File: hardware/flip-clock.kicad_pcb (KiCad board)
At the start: 2 copper layers, 68.1 x 38.6 mm, 9 parts, among them J1 Screw_Terminal_01x02, U1 ESP-01v090, U2 AP1117-33

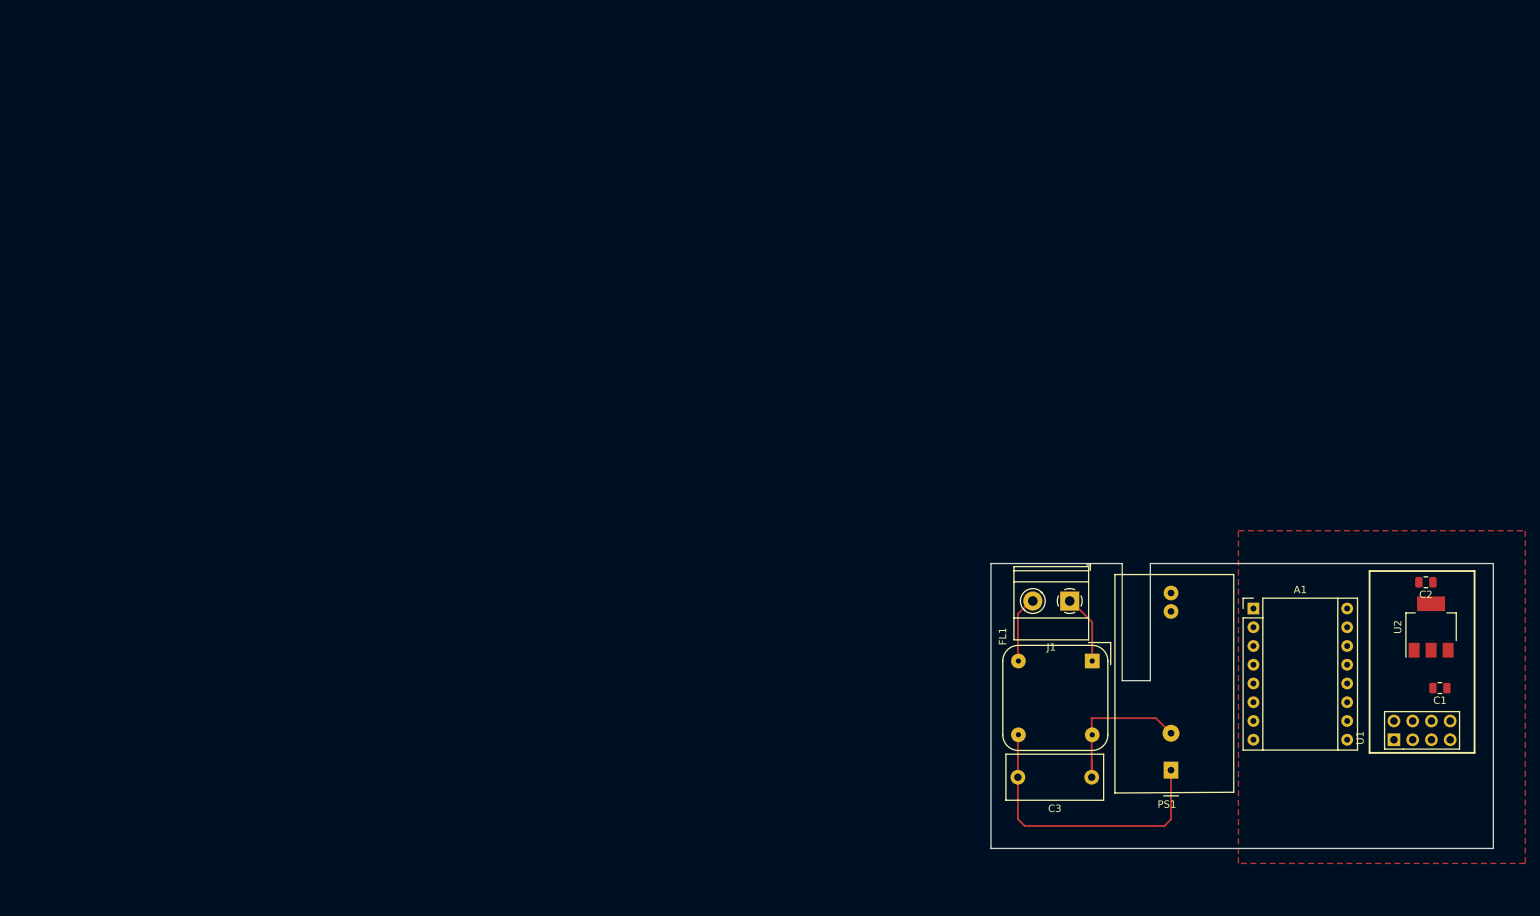
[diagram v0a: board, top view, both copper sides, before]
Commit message: Layout without choke
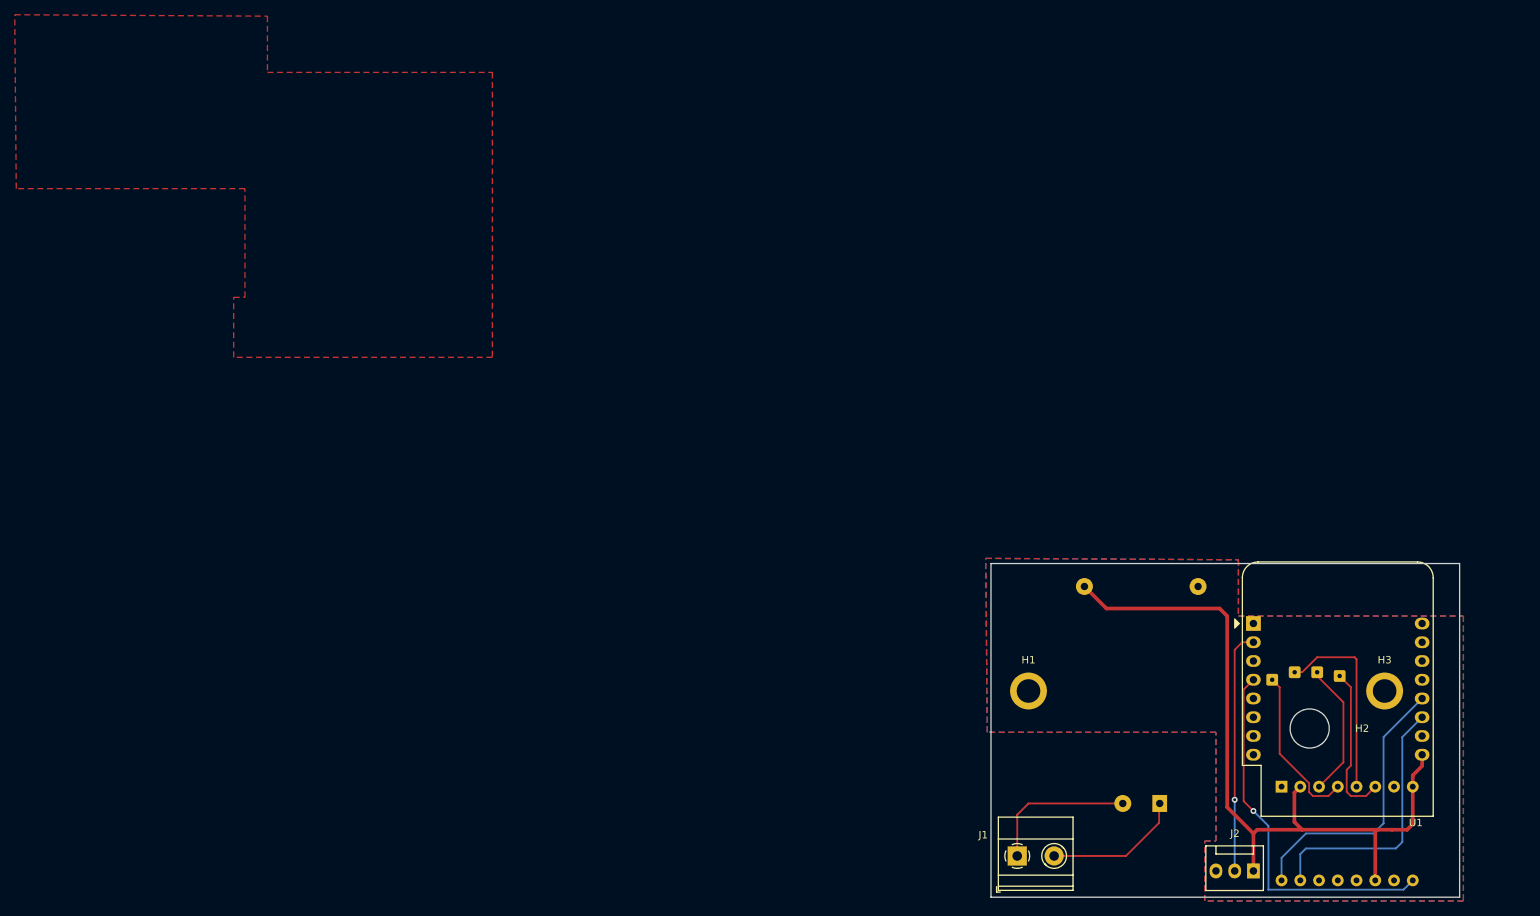
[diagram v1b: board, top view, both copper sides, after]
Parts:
- removed C1, C2: C, Capacitor_SMD:C_0805_2012Metric
- removed C3: C, Capacitor_THT:C_Rect_L13.0mm_W6.0mm_P10.00mm_FKS3_FKP3_MKS4
- removed FL1: Choke_Schaffner_RN102-0.3-02-12M, Inductor_THT:Choke_Schaffner_RN102-04-14.0x14.0mm
- removed U2: AP1117-33, Package_TO_SOT_SMD:SOT-223-3_TabPin2
- added H-1A1: MountingHole_Pad, Connector_Wire:SolderWire-0.1sqmm_1x01_D0.4mm_OD1mm, B.Cu at (160.0, 66.5)
- added H-1B1: MountingHole_Pad, Connector_Wire:SolderWire-0.1sqmm_1x01_D0.4mm_OD1mm, B.Cu at (166.1, 65.5)
- added H-2A1: MountingHole_Pad, Connector_Wire:SolderWire-0.1sqmm_1x01_D0.4mm_OD1mm, B.Cu at (163.1, 65.5)
- added H-2B1: MountingHole_Pad, Connector_Wire:SolderWire-0.1sqmm_1x01_D0.4mm_OD1mm, B.Cu at (169.2, 66.0)
- added H1: MountingHole, MountingHole:MountingHole_3.2mm_M3, F.Cu at (127.0, 68.1)
- added H2: MountingHole, MountingHole:MountingHole_5.3mm_M5, F.Cu at (165.1, 73.2)
- added H3: MountingHole, MountingHole:MountingHole_3.2mm_M3, F.Cu at (175.3, 68.1)
- added J2: Conn_01x03_Female, Connector:FanPinHeader_1x03_P2.54mm_Vertical, F.Cu at (157.5, 92.5)
- A1: moved to B.Cu
- PS1: footprint Converter_ACDC:Converter_ACDC_HiLink_HLK-2Mxx -> Converter_ACDC:Converter_ACDC_HiLink_HLK-PMxx; moved to B.Cu
- U1: value ESP-01v090 -> WeMos_D1_mini; footprint ESP:ESP-01 -> Module:WEMOS_D1_mini_light
- moved J1 35.3 mm to (125.5, 90.4), turned to 0 degrees
- moved U1 24.7 mm to (157.5, 58.9), turned to 0 degrees
- moved A1 24.4 mm to (161.3, 81.0), turned to -90 degrees
- moved PS1 4.11 mm to (144.8, 83.3)
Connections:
- A1 pad 10: /3V3 -> unconnected-(A1-Pad10)
- A1 pad 11: /3V3 -> VCC
- A1 pad 12: /3V3 -> unconnected-(A1-Pad12)
- A1 pad 13: Net-(A1-Pad13) -> unconnected-(A1-Pad13)
- A1 pad 16: GND -> /DIR
- A1 pad 2: /3V3 -> VCC
- A1 pad 3: unconnected-(A1-Pad3) -> /1B
- A1 pad 4: unconnected-(A1-Pad4) -> /1A
- A1 pad 5: unconnected-(A1-Pad5) -> /2A
- A1 pad 6: unconnected-(A1-Pad6) -> /2B
- A1 pad 9: GND -> //ENABLE
- J1 pad 1: Net-(FL1-Pad1) -> /AC1
- J1 pad 2: Net-(FL1-Pad3) -> /AC2
- PS1 pad 1: Net-(PS1-Pad1) -> /AC2
- PS1 pad 2: Net-(PS1-Pad2) -> /AC1
- U1 pad 1: Net-(A1-Pad13) -> unconnected-(U1-Pad1)
- U1 pad 2: GND -> /PD_IN
- U1 pad 4: /STEP -> //ENABLE
- U1 pad 7: /3V3 -> unconnected-(U1-Pad7)
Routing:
- net VCC: track 0.00 -> 102.6 mm
- net //ENABLE: track 0.00 -> 50.5 mm, vias 0 -> 1
- net Net-(PS1-Pad1): track 39.6 -> 0.00 mm
- net /DIR: track 0.00 -> 37.9 mm
- net /STEP: track 0.00 -> 36.1 mm
- net /PD_IN: track 0.00 -> 32.9 mm, vias 0 -> 1
- net /2A: track 0.00 -> 26.6 mm
- net /1A: track 0.00 -> 21.9 mm
- net Net-(PS1-Pad2): track 21.9 -> 0.00 mm
- net /2B: track 0.00 -> 21.2 mm
- net /AC1: track 0.00 -> 20.4 mm
- net /AC2: track 0.00 -> 18.7 mm
- net /1B: track 0.00 -> 18.3 mm
- net Net-(FL1-Pad1): track 9.49 -> 0.00 mm
- net Net-(FL1-Pad3): track 8.16 -> 0.00 mm
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- added copper zone on B.Cu, net GND
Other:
- board size 68.1 x 38.6 mm -> 63.5 x 45.2 mm

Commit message: Trapezoid Layout, Transformer in Front
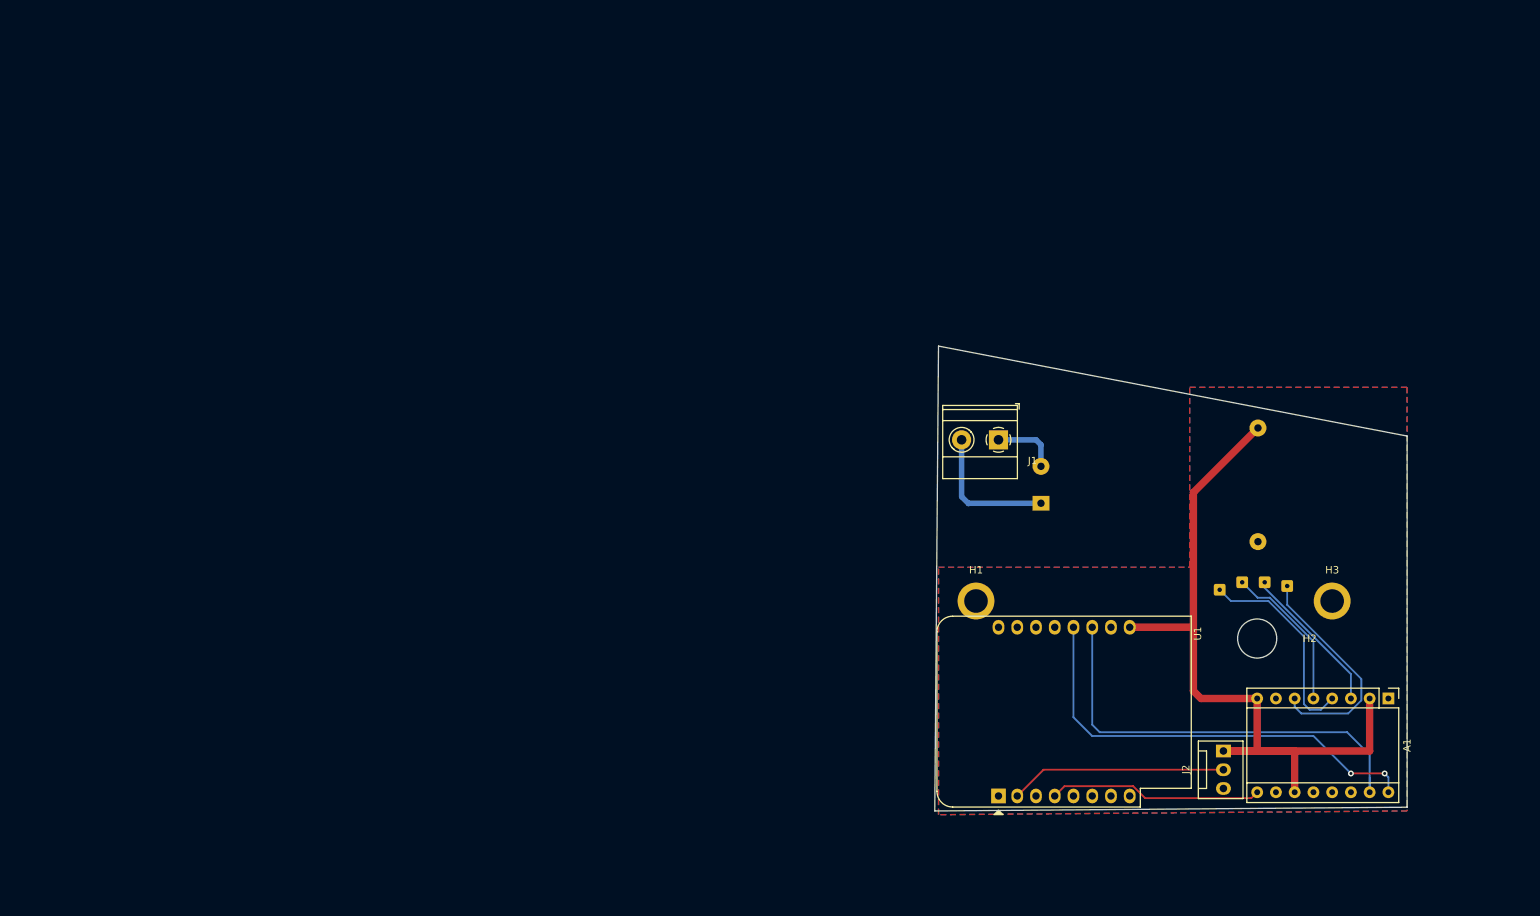
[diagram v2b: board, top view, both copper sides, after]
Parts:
- A1: moved to F.Cu
- moved J1 56.4 mm to (122.9, 34.0), turned to 180 degrees
- moved PS1 43.7 mm to (128.7, 42.6), turned to 0 degrees
- moved U1 41.7 mm to (122.9, 82.3), turned to 90 degrees
- moved A1 18.8 mm to (175.8, 69.1)
- moved J2 16.8 mm to (153.4, 76.2), turned to -90 degrees
- moved H-1A1 14.1 mm to (152.9, 54.4)
- moved H-1B1 14.1 mm to (159.0, 53.3)
- moved H-2A1 14.1 mm to (156.0, 53.3)
- moved H-2B1 14.1 mm to (162.1, 53.8)
- moved H1 14.1 mm to (119.9, 55.9)
- moved H2 14.1 mm to (158.0, 61.0)
- moved H3 14.1 mm to (168.1, 55.9)
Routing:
- net /STEP: track 36.1 -> 59.6 mm
- net /DIR: track 37.9 -> 60.3 mm, vias 0 -> 2
- net //ENABLE: track 50.5 -> 29.0 mm, vias 1 -> 0
- net /AC1: track 20.4 -> 8.96 mm
- net /2B: track 21.2 -> 30.9 mm
- net VCC: track 102.6 -> 111.5 mm
- net /1A: track 21.9 -> 28.0 mm
- net /2A: track 26.6 -> 20.7 mm
- net /PD_IN: track 32.9 -> 29.4 mm, vias 1 -> 0
- net /1B: track 18.3 -> 20.6 mm
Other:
- board size 63.5 x 45.2 mm -> 64 x 63 mm

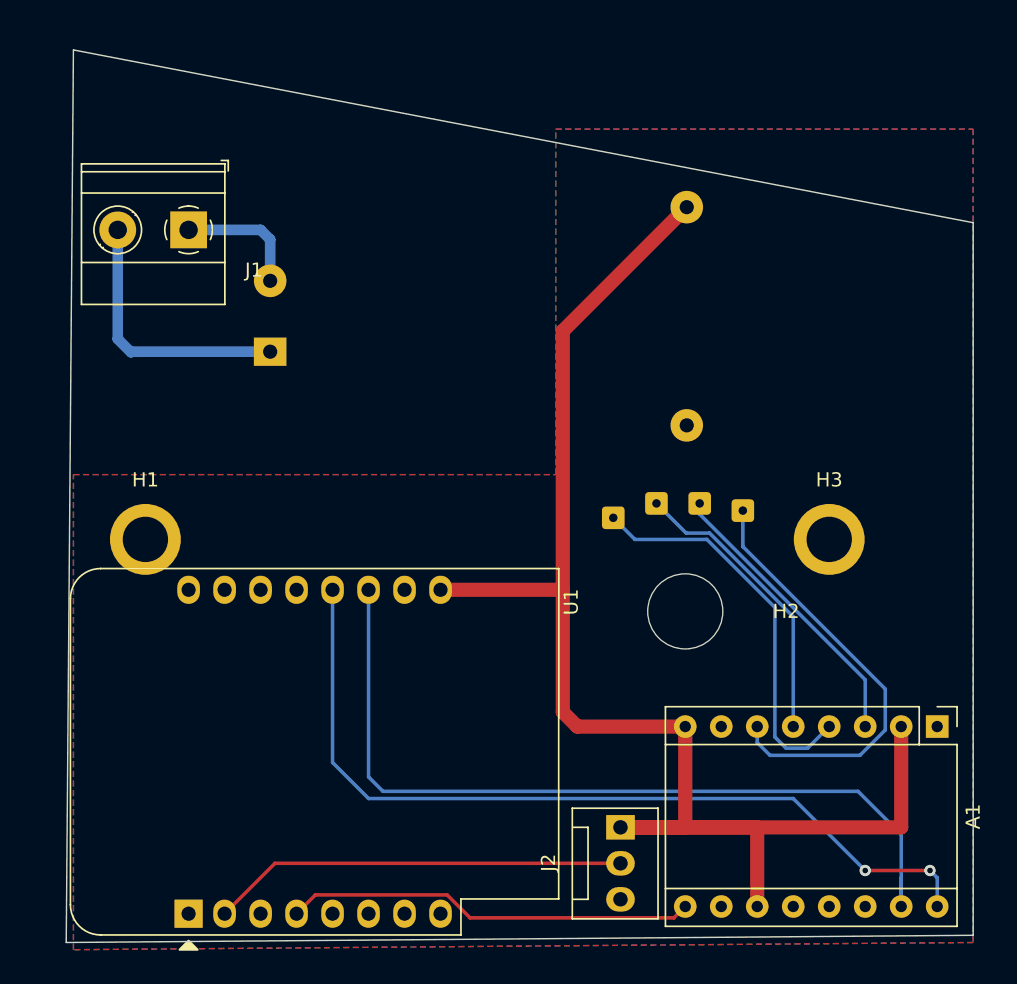
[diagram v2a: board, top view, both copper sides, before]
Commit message: Wrong side populated
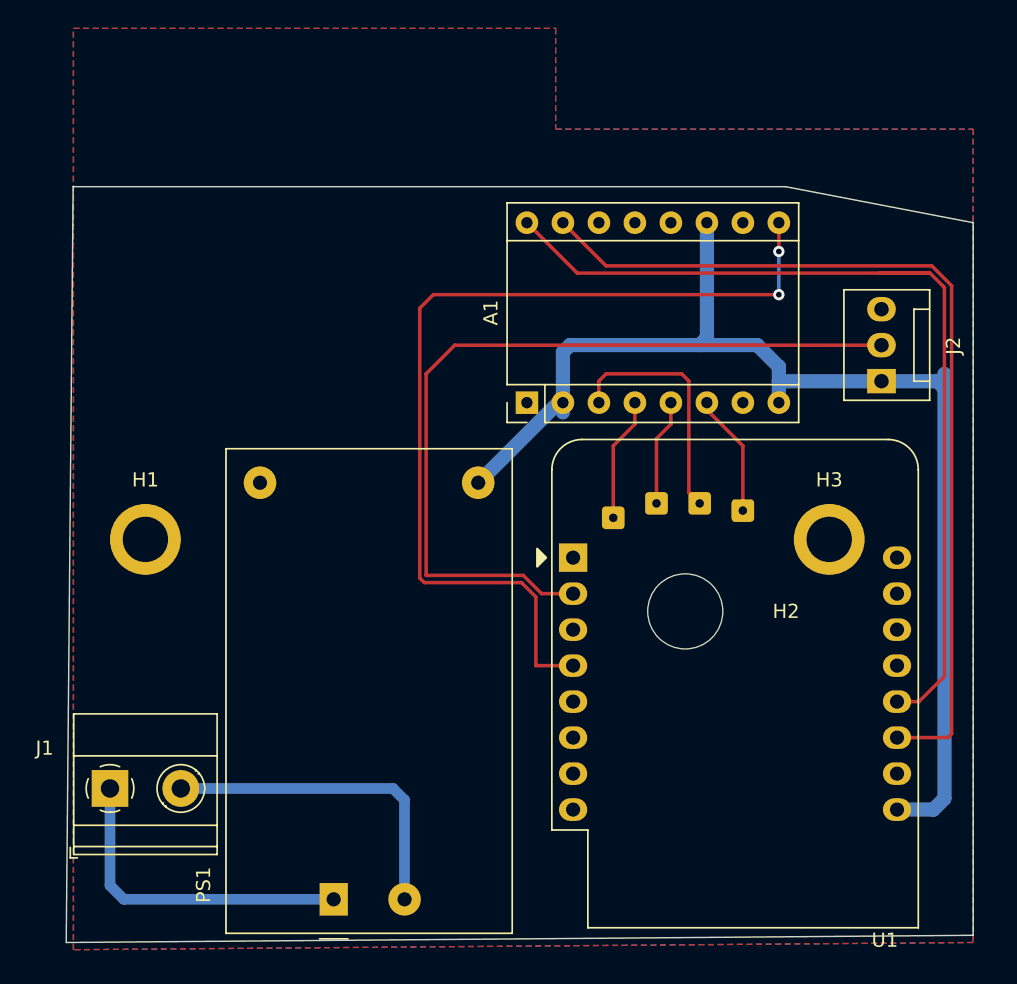
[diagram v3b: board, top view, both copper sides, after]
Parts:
- PS1: moved to F.Cu
- moved J1 39.8 mm to (117.4, 73.5), turned to 0 degrees
- moved PS1 38.9 mm to (133.2, 81.3), turned to 90 degrees
- moved U1 37.0 mm to (150.1, 57.2), turned to 0 degrees
- moved A1 36.9 mm to (146.8, 46.2), turned to 90 degrees
- moved J2 36.5 mm to (171.8, 44.7), turned to 90 degrees
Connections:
- J1 pad 1: /AC1 -> /AC2
- J1 pad 2: /AC2 -> /AC1
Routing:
- net //ENABLE: track 29.0 -> 66.1 mm, vias 0 -> 2
- net /PD_IN: track 29.4 -> 58.1 mm
- net VCC: track 111.5 -> 85.7 mm
- net /2B: track 30.9 -> 8.67 mm
- net /1A: track 28.0 -> 8.76 mm
- net /AC1: track 8.96 -> 23.1 mm
- net /2A: track 20.7 -> 7.53 mm
- net /DIR: track 60.3 -> 66.6 mm, vias 2 -> 0
- net /STEP: track 59.6 -> 64.9 mm
- net /AC2: track 18.9 -> 23.0 mm
- net /1B: track 20.6 -> 17.2 mm
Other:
- board size 64 x 63 mm -> 64 x 53.3 mm

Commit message: Correct side
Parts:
- A1, H1, H3, J1, J2, PS1, U1: moved to B.Cu
- moved U1 22.6 mm to (172.7, 57.2), turned to 180 degrees
- moved A1 18.3 mm to (165.1, 46.2)
- moved PS1 4.96 mm to (138.1, 81.1)
- moved J1 4.53 mm to (121.9, 73.4), turned to 180 degrees
- moved J2 2.20 mm to (171.4, 42.5)
- turned H1 to 180 degrees
- turned H3 to 180 degrees
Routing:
- net /PD_IN: track 58.1 -> 27.1 mm
- net VCC: track 85.7 -> 108.7 mm
- net /2B: track 8.67 -> 23.5 mm
- net /DIR: track 66.6 -> 52.2 mm, vias 0 -> 1
- net /1B: track 17.2 -> 7.53 mm
- net /STEP: track 64.9 -> 59.2 mm
- net //ENABLE: track 66.1 -> 69.1 mm, vias 2 -> 1
- net /1A: track 8.76 -> 11.5 mm
- net /AC1: track 23.1 -> 23.7 mm
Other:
- board size 64 x 53.3 mm -> 64.6 x 53.3 mm

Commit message: Pre-Production
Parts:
- added R1: 4k7, Resistor_SMD:R_0805_2012Metric, F.Cu at (168.1, 38.6)
- H1, H3: footprint MountingHole:MountingHole_3.2mm_M3 -> MountingHole:MountingHole_3.2mm_M3_Pad
- J2: value Conn_01x03_Female -> Conn_01x04; footprint Connector:FanPinHeader_1x03_P2.54mm_Vertical -> Connector_Wire:SolderWire-0.1sqmm_1x04_P3.6mm_D0.4mm_OD1mm; moved to F.Cu
- moved J2 3.50 mm to (171.7, 46.0)
- moved U1 0.51 mm to (173.2, 57.2)
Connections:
- J2 pad 3: GND -> /HOUR
- U1 pad 13: unconnected-(U1-Pad13) -> /SDA
- U1 pad 14: unconnected-(U1-Pad14) -> /SCL
- U1 pad 3: unconnected-(U1-Pad3) -> /HOUR
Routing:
- net /HOUR: track 0.00 -> 32.4 mm
- net VCC: track 108.7 -> 120.2 mm
- net /PD_IN: track 27.1 -> 22.6 mm
- net //ENABLE: track 69.1 -> 69.6 mm
- net /STEP: track 59.2 -> 58.7 mm
